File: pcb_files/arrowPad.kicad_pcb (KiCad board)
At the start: 2 copper layers, 90.2 x 90.2 mm, 65 parts, among them J1 AudioJack3_Ground, J2 AudioJack3_Ground, K1 KEYSW, K10 KEYSW, K11 KEYSW, K12 KEYSW, K13 KEYSW, K14 KEYSW, K15 KEYSW, K16 KEYSW, K2 KEYSW, K3 KEYSW, K4 KEYSW, K5 KEYSW, K6 KEYSW, K7 KEYSW, K8 KEYSW, K9 KEYSW, U1 ProMicro, U2 NRF24L01_Breakout, U3 ADG417BN, U4 AMS1117-3.3, U5 ADG417BN, U6 ADG417BN, U7 TLC5940PWP

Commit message: cleaned up board text
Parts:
- BT1, U3, U5, U6: moved to B.Cu
- D28: value LED -> LED - +
- turned BT1 to 180 degrees
- turned U3 to 0 degrees
- turned U5 to 180 degrees
- turned U6 to 270 degrees

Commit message: cleand up traces
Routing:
- net Net-(J1-Pad1): track 181.4 -> 179.8 mm
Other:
- board text added: "By: LowJ"
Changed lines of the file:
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@@
   (general
     (thickness 1.6)
-    (drawings 16)
-    (tracks 1122)
+    (drawings 17)
+    (tracks 1121)
     (zones 0)
     (modules 65)
@@
     (descr "Kailh \"Choc\" PG1350 keyswitch socket mount")
     (tags kailh,choc)
-    (fp_text reference K8 (at 0 8.3) (layer B.SilkS)
+    (fp_text reference K8 (at 0 -5.08) (layer B.SilkS)
       (effects (font (size 1 1) (thickness 0.15)) (justify mirror))
     )
@@
     (descr "Kailh \"Choc\" PG1350 keyswitch socket mount")
     (tags kailh,choc)
-    (fp_text reference K6 (at 0 8.3) (layer B.SilkS)
+    (fp_text reference K6 (at 0 -5.08) (layer B.SilkS)
       (effects (font (size 1 1) (thickness 0.15)) (justify mirror))
     )
@@
     (descr "Kailh \"Choc\" PG1350 keyswitch socket mount")
     (tags kailh,choc)
-    (fp_text reference K1 (at 0 8.3) (layer B.SilkS)
+    (fp_text reference K1 (at 0 -5.08) (layer B.SilkS)
       (effects (font (size 1 1) (thickness 0.15)) (justify mirror))
     )
@@
     (descr "Kailh \"Choc\" PG1350 keyswitch socket mount")
     (tags kailh,choc)
-    (fp_text reference K2 (at 0 8.3) (layer B.SilkS)
+    (fp_text reference K2 (at 0 -5.124) (layer B.SilkS)
       (effects (font (size 1 1) (thickness 0.15)) (justify mirror))
     )
@@
     (descr "Kailh \"Choc\" PG1350 keyswitch socket mount")
     (tags kailh,choc)
-    (fp_text reference K3 (at 0 8.3) (layer B.SilkS)
+    (fp_text reference K3 (at 0 -3.81) (layer B.SilkS)
       (effects (font (size 1 1) (thickness 0.15)) (justify mirror))
     )
@@
     (descr "Kailh \"Choc\" PG1350 keyswitch socket mount")
     (tags kailh,choc)
-    (fp_text reference K4 (at 0 8.3) (layer B.SilkS)
+    (fp_text reference K4 (at 0 -3.81) (layer B.SilkS)
       (effects (font (size 1 1) (thickness 0.15)) (justify mirror))
     )
@@
     (descr "Kailh \"Choc\" PG1350 keyswitch socket mount")
     (tags kailh,choc)
-    (fp_text reference K5 (at 0 8.3) (layer B.SilkS)
+    (fp_text reference K5 (at 0 -5.08) (layer B.SilkS)
       (effects (font (size 1 1) (thickness 0.15)) (justify mirror))
     )
@@
     (descr "Kailh \"Choc\" PG1350 keyswitch socket mount")
     (tags kailh,choc)
-    (fp_text reference K7 (at 0 8.3) (layer B.SilkS)
+    (fp_text reference K7 (at 0 -5.08) (layer B.SilkS)
       (effects (font (size 1 1) (thickness 0.15)) (justify mirror))
     )
@@
     (descr "Kailh \"Choc\" PG1350 keyswitch socket mount")
     (tags kailh,choc)
-    (fp_text reference K9 (at 0 8.3) (layer B.SilkS)
+    (fp_text reference K9 (at 0 -5.08) (layer B.SilkS)
       (effects (font (size 1 1) (thickness 0.15)) (justify mirror))
     )
@@
     (descr "Through hole straight pin header, 1x03, 2.54mm pitch, single row")
     (tags "Through hole pin header THT 1x03 2.54mm single row")
-    (fp_text reference U3 (at 0 2.865 270) (layer B.SilkS)
+    (fp_text reference U3 (at 0 -7.0866) (layer B.SilkS)
       (effects (font (size 1 1) (thickness 0.15)) (justify mirror))
     )
@@
     (descr "Kailh \"Choc\" PG1350 keyswitch socket mount")
     (tags kailh,choc)
-    (fp_text reference K10 (at 0 8.3) (layer B.SilkS)
+    (fp_text reference K10 (at 0 -5.08) (layer B.SilkS)
       (effects (font (size 1 1) (thickness 0.15)) (justify mirror))
     )
@@
     (descr "Kailh \"Choc\" PG1350 keyswitch socket mount")
     (tags kailh,choc)
-    (fp_text reference K11 (at 0 8.3) (layer B.SilkS)
+    (fp_text reference K11 (at 0 -5.08) (layer B.SilkS)
       (effects (font (size 1 1) (thickness 0.15)) (justify mirror))
     )
@@
     (descr "Kailh \"Choc\" PG1350 keyswitch socket mount")
     (tags kailh,choc)
-    (fp_text reference K12 (at 0 8.3) (layer B.SilkS)
+    (fp_text reference K12 (at 0 -5.08) (layer B.SilkS)
       (effects (font (size 1 1) (thickness 0.15)) (justify mirror))
     )
@@
     (descr "Kailh \"Choc\" PG1350 keyswitch socket mount")
     (tags kailh,choc)
-    (fp_text reference K13 (at 0 8.3) (layer B.SilkS)
+    (fp_text reference K13 (at 0 -5.08) (layer B.SilkS)
       (effects (font (size 1 1) (thickness 0.15)) (justify mirror))
     )
@@
     (descr "Kailh \"Choc\" PG1350 keyswitch socket mount")
     (tags kailh,choc)
-    (fp_text reference K14 (at 0 8.3) (layer B.SilkS)
+    (fp_text reference K14 (at 0 -5.08) (layer B.SilkS)
       (effects (font (size 1 1) (thickness 0.15)) (justify mirror))
     )
@@
     (descr "Kailh \"Choc\" PG1350 keyswitch socket mount")
     (tags kailh,choc)
-    (fp_text reference K15 (at 0 8.3) (layer B.SilkS)
+    (fp_text reference K15 (at 0 -5.08) (layer B.SilkS)
       (effects (font (size 1 1) (thickness 0.15)) (justify mirror))
     )
@@
     (descr "Kailh \"Choc\" PG1350 keyswitch socket mount")
     (tags kailh,choc)
-    (fp_text reference K16 (at 0 8.3) (layer B.SilkS)
+    (fp_text reference K16 (at 0 -5.08) (layer B.SilkS)
       (effects (font (size 1 1) (thickness 0.15)) (justify mirror))
     )
@@
     (pad 1 np_thru_hole circle (at 0 0) (size 3.2 3.2) (drill 3.2) (layers *.Cu *.Mask))
   )
+  (gr_text "By: LowJ" (at 116.84 124.46 90) (layer F.SilkS)
+    (effects (font (size 1.5 1.5) (thickness 0.3)))
+  )
   (gr_line (start 204.47 133.985) (end 204.47 73.66) (layer Edge.Cuts) (width 0.15))
   (gr_line (start 204.47 52.705) (end 204.47 58.42) (layer Edge.Cuts) (width 0.15))
@@
   (via (at 142.24 63.5) (size 0.8) (drill 0.4) (layers F.Cu B.Cu) (net 0))
   (via (at 142.24 64.77) (size 0.8) (drill 0.4) (layers F.Cu B.Cu) (net 0))
-  (via (at 132.461 59.944) (size 0.8) (drill 0.4) (layers F.Cu B.Cu) (net 40))
   (segment (start 197.206501 81.166601) (end 197.166601 81.166601) (width 0.25) (layer B.Cu) (net 1) (status 10))
   (segment (start 198.0565 82.0166) (end 197.206501 81.166601) (width 0.25) (layer B.Cu) (net 1) (status 30))
@@
   (segment (start 147.32 54.61) (end 146.05 53.34) (width 0.25) (layer F.Cu) (net 2))
   (segment (start 147.32 55.88) (end 147.32 54.61) (width 0.25) (layer F.Cu) (net 2))
-  (segment (start 122.7796 81.1223) (end 122.8546 81.0473) (width 0.25) (layer B.Cu) (net 67))
   (via (at 191.262 104.394) (size 0.8) (drill 0.4) (layers F.Cu B.Cu) (net 2))
   (via (at 133.858 62.484) (size 0.8) (drill 0.4) (layers F.Cu B.Cu) (net 2))
@@
   (segment (start 141.585 108.17) (end 145.81 112.395) (width 0.25) (layer B.Cu) (net 28) (status 20))
   (segment (start 141.585 106.62) (end 141.585 108.17) (width 0.25) (layer B.Cu) (net 28) (status 10))
-  (segment (start 123.5041 93.1883) (end 123.5041 94.8383) (width 0.25) (layer B.Cu) (net 30) (status 10))
   (segment (start 125 118) (end 125 120) (width 0.25) (layer F.Cu) (net 30))
   (segment (start 125 120) (end 125.5 120.5) (width 0.25) (layer F.Cu) (net 30))
@@
   (segment (start 179.685 127.22) (end 183.91 131.445) (width 0.25) (layer B.Cu) (net 39) (status 20))
   (segment (start 179.685 125.67) (end 179.685 127.22) (width 0.25) (layer B.Cu) (net 39) (status 10))
+  (via (at 132.461 59.944) (size 0.8) (drill 0.4) (layers F.Cu B.Cu) (net 40))
   (segment (start 118.694517 63.25229) (end 118.694517 72.194517) (width 0.25) (layer B.Cu) (net 40))
   (segment (start 126.785001 55.459999) (end 126.486808 55.459999) (width 0.25) (layer B.Cu) (net 40) (status 10))
@@
   (segment (start 146 85.5) (end 142.5 85.5) (width 0.25) (layer F.Cu) (net 64))
   (segment (start 128.5546 79.0973) (end 126.675 79.0973) (width 0.25) (layer B.Cu) (net 64))
+  (segment (start 122.7796 81.1223) (end 122.8546 81.0473) (width 0.25) (layer B.Cu) (net 67))
   (segment (start 128.5546 80.3973) (end 131.9593 80.3973) (width 0.25) (layer B.Cu) (net 68))
   (via (at 133.477 81.915) (size 0.8) (drill 0.4) (layers F.Cu B.Cu) (net 68))

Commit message: added image for pcb
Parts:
- removed the REF** at (200.0, 52.7)
- removed the REF** at (118.7, 52.7)
- removed the REF** at (118.7, 134.0)
- removed the REF** at (200.0, 134.0)
- added REF**: MountingHole_3.2mm_M3, MountingHole:MountingHole_3.2mm_M3, F.Cu at (118.7, 134.0)
- added REF**: MountingHole_3.2mm_M3, MountingHole:MountingHole_3.2mm_M3, F.Cu at (118.6, 52.6)
- added REF**: MountingHole_3.2mm_M3, MountingHole:MountingHole_3.2mm_M3, F.Cu at (200.2, 52.6)
- added REF**: MountingHole_3.2mm_M3, MountingHole:MountingHole_3.2mm_M3, F.Cu at (200.2, 134.0)
- D28: value LED - + -> LED
- U4: footprint promicro:AMS1117flipped -> AMS1117-3.3:SOT229P700X180-4N; moved to B.Cu
- moved R1 14.2 mm to (202.6, 78.5)
- moved J1 8.17 mm to (195.2, 96.8)
- moved J2 7.07 mm to (123.6, 96.9)
- turned U4 to 0 degrees
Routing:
- net Net-(J1-Pad1): track 179.8 -> 198.6 mm
- net Net-(J1-Pad2): track 127.9 -> 145.1 mm, vias 3 -> 5
- net Net-(R1-Pad2): track 135.0 -> 151.4 mm, vias 3 -> 4
- net /VCC1: track 470.2 -> 481.3 mm
- net Net-(U4-Pad3): track 8.20 -> 15.5 mm, vias 0 -> 2
- net /GND1: track 23.8 -> 17.2 mm, vias 13 -> 11
- net /Row4: track 165.8 -> 172.0 mm, vias 0 -> 3
- net /Col1: track 129.6 -> 135.8 mm
- net /RAW1: track 196.4 -> 191.3 mm
- net Net-(D20-Pad2): track 38.0 -> 42.3 mm
- net Net-(D32-Pad2): track 115.0 -> 117.3 mm
- net Net-(D35-Pad2): track 49.7 -> 51.8 mm
- net Net-(D34-Pad2): track 72.7 -> 74.7 mm
- net Net-(U1-Pad12): track 90.4 -> 92.3 mm
- net Net-(D33-Pad2): track 93.8 -> 95.5 mm
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
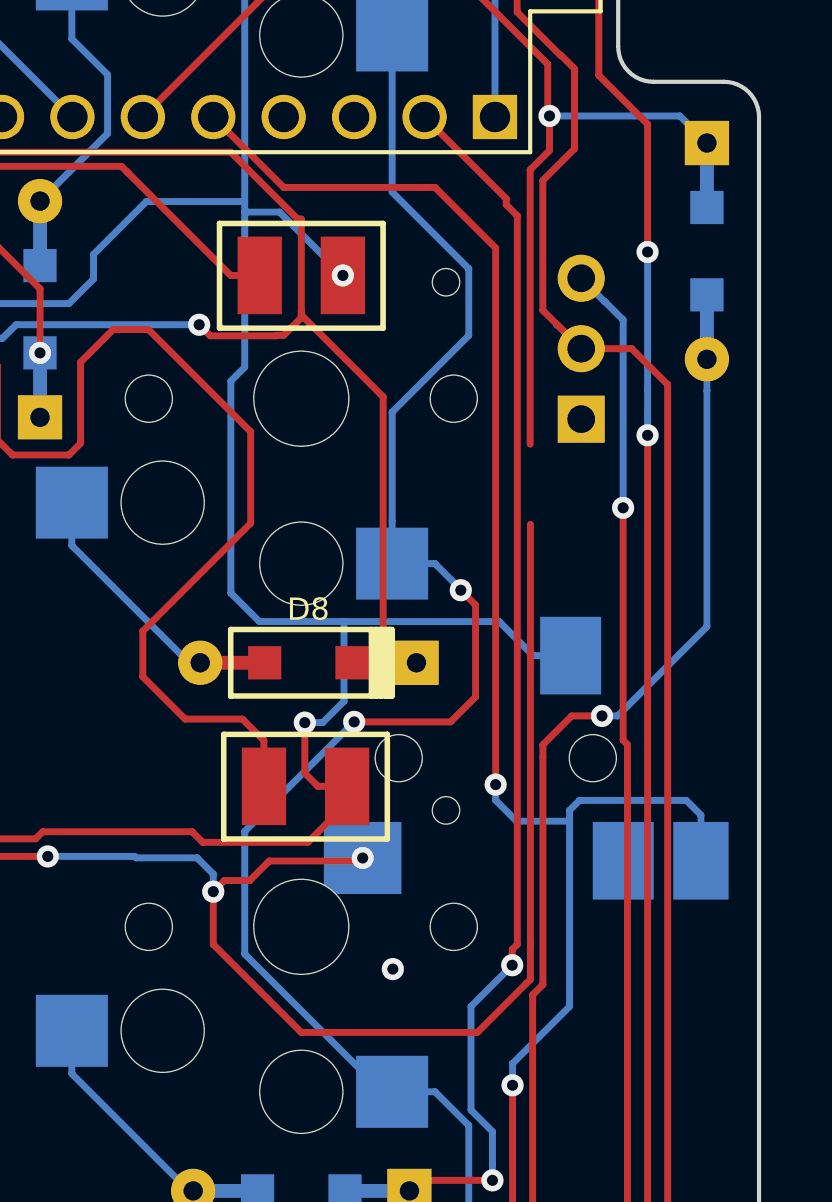
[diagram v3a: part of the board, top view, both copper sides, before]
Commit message: snorlax in silk screen
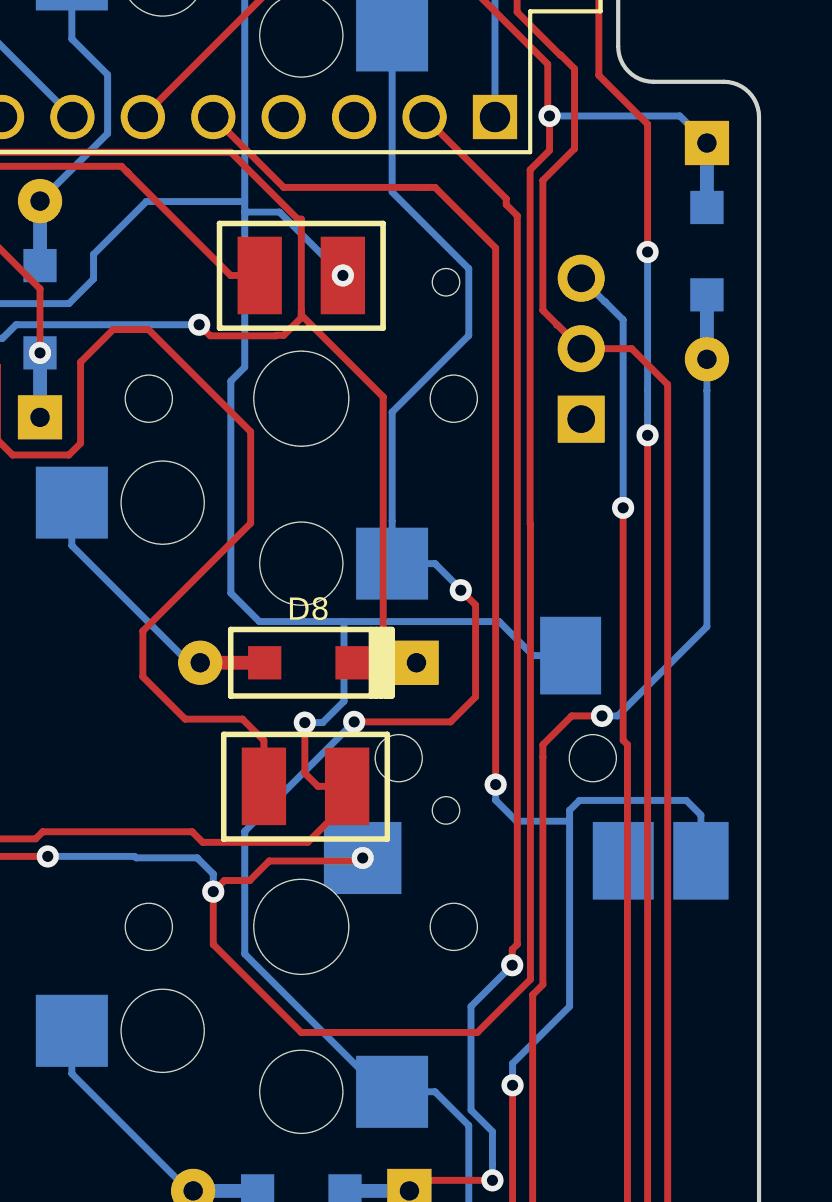
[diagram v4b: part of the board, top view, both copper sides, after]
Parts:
- added G***: LOGO, snorlax:s2, B.Cu at (160.0, 97.8)
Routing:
- net Net-(J1-Pad2): track 145.1 -> 148.0 mm
- net /GND1: vias 11 -> 10

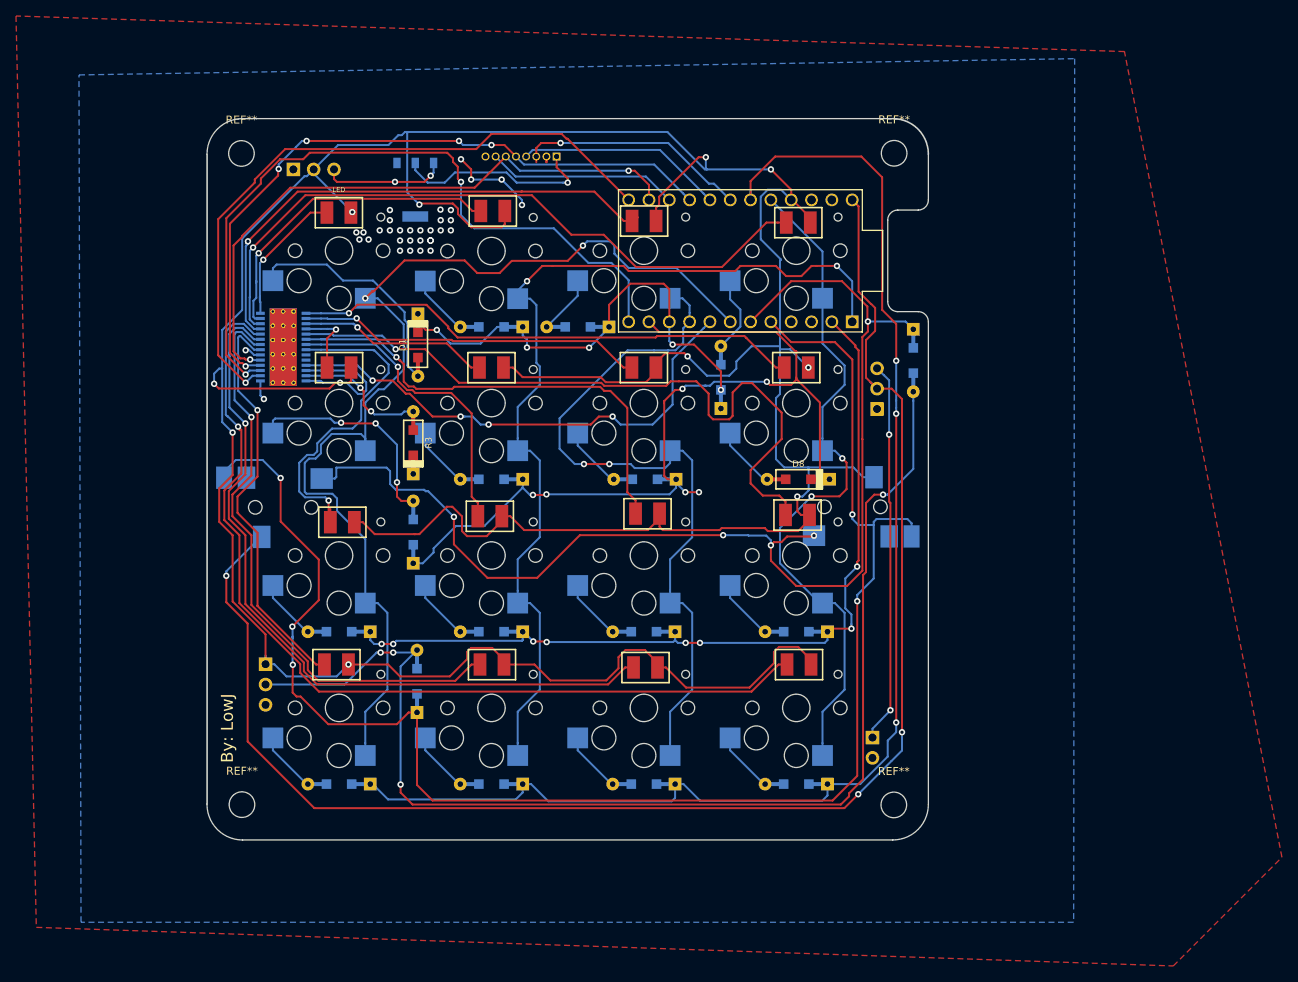
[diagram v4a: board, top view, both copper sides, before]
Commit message: fixed unconnected grounds
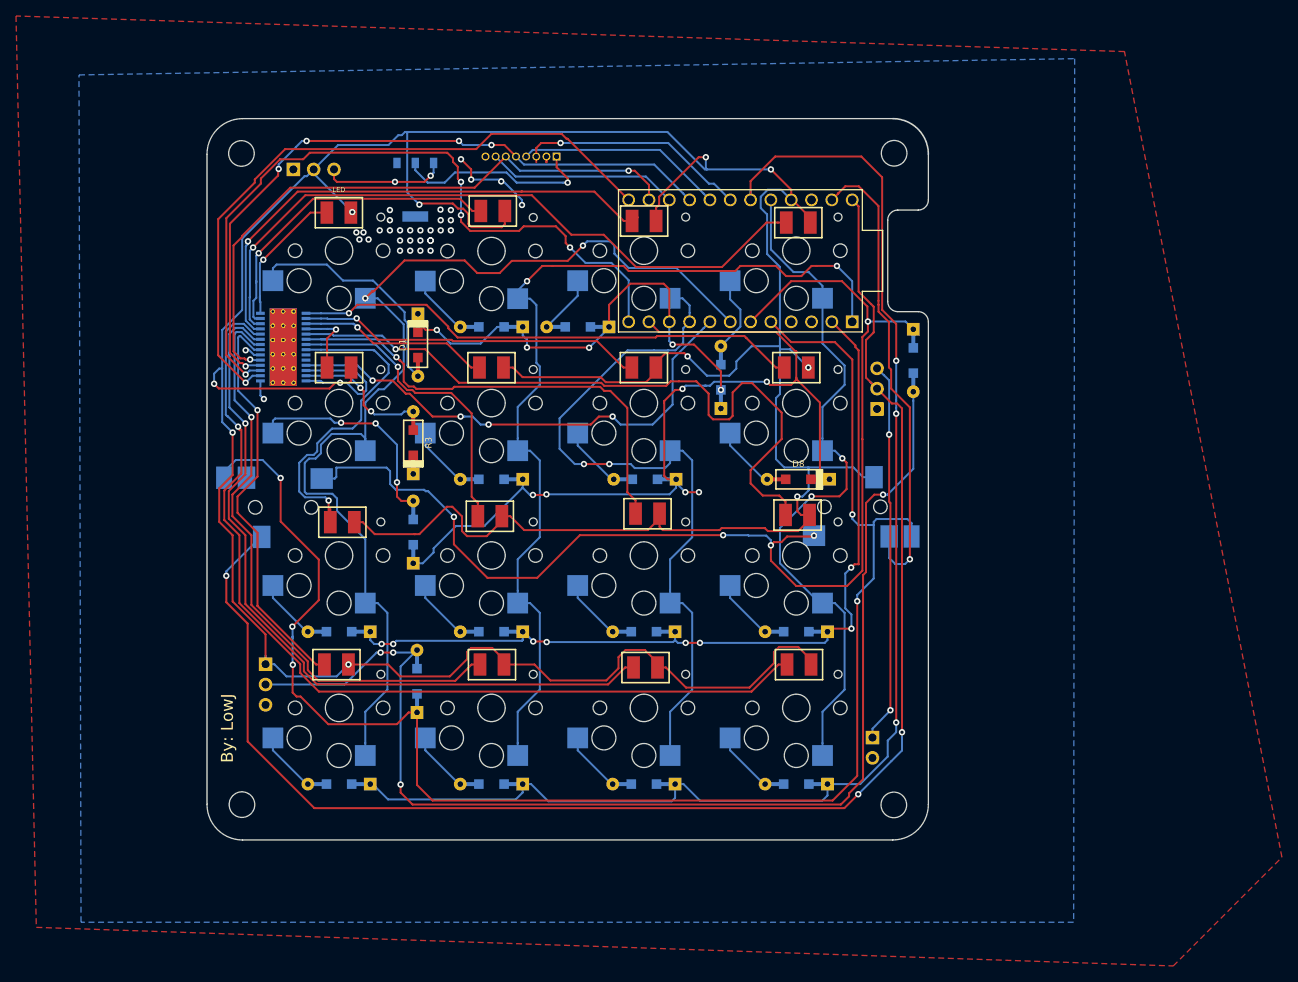
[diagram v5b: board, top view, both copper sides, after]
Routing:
- net /GND1: track 17.2 -> 76.4 mm, vias 10 -> 11
- net Net-(U1-Pad12): track 92.3 -> 93.7 mm, vias 2 -> 4
- net /Col4: track 87.8 -> 88.9 mm
- net /RAW1: track 191.3 -> 190.5 mm
